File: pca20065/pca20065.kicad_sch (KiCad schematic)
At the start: 7 parts

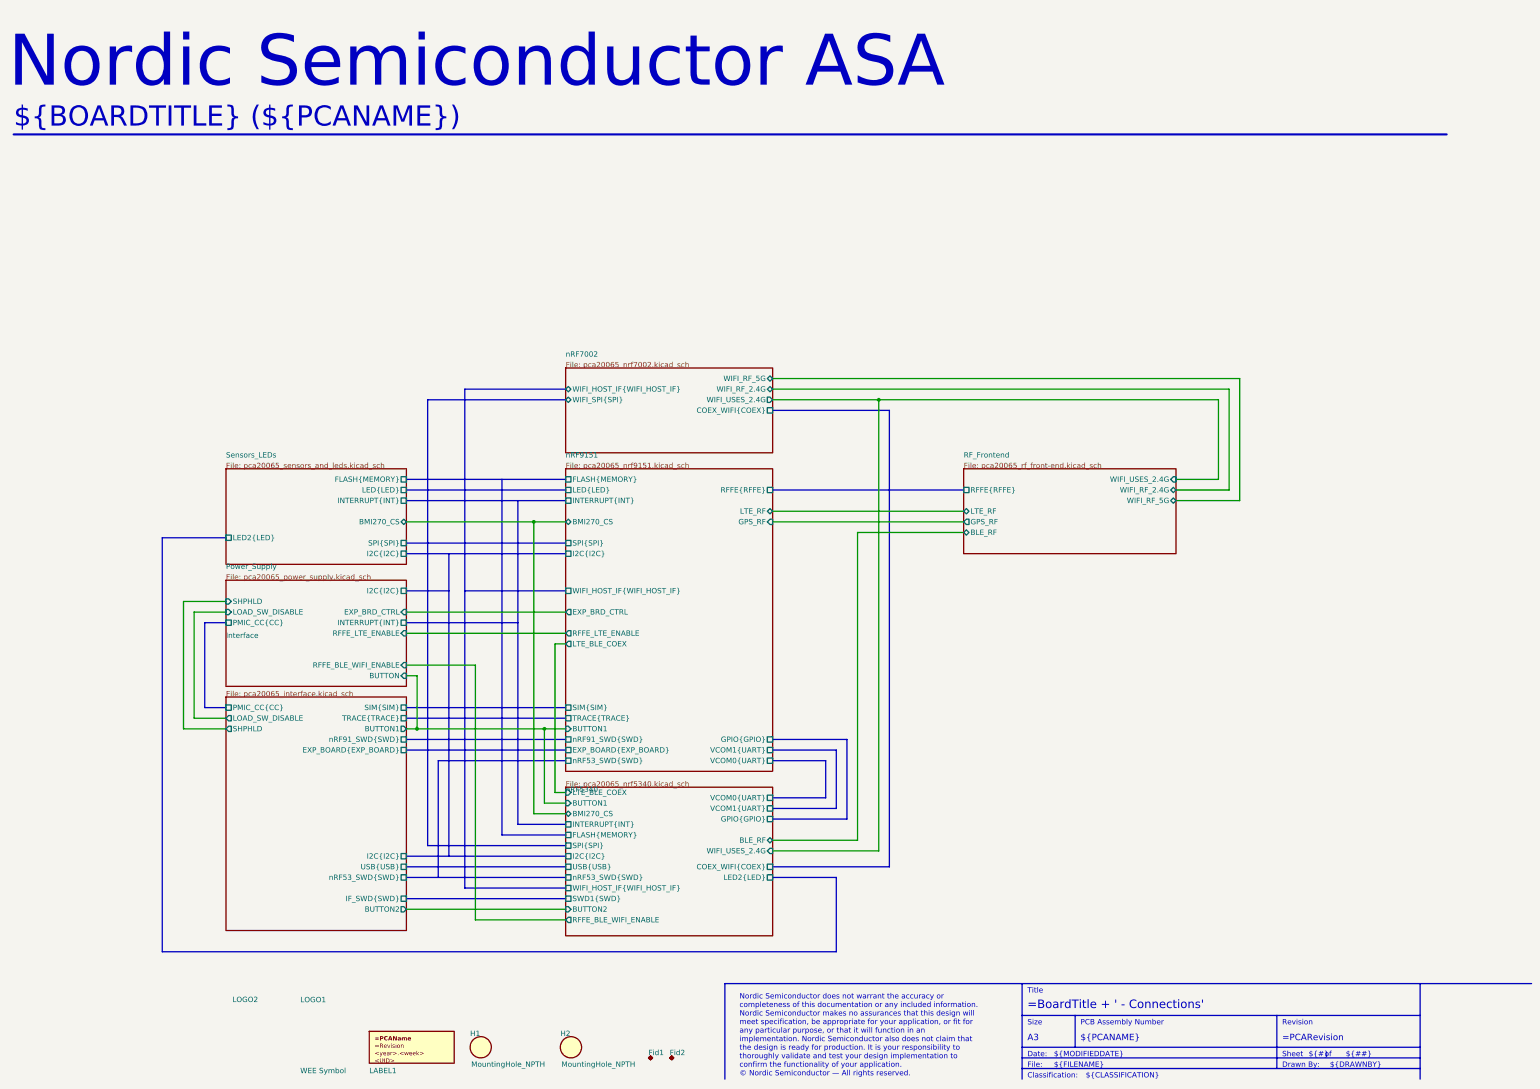
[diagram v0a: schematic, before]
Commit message: Replaced nrf5340 with nrf54l15
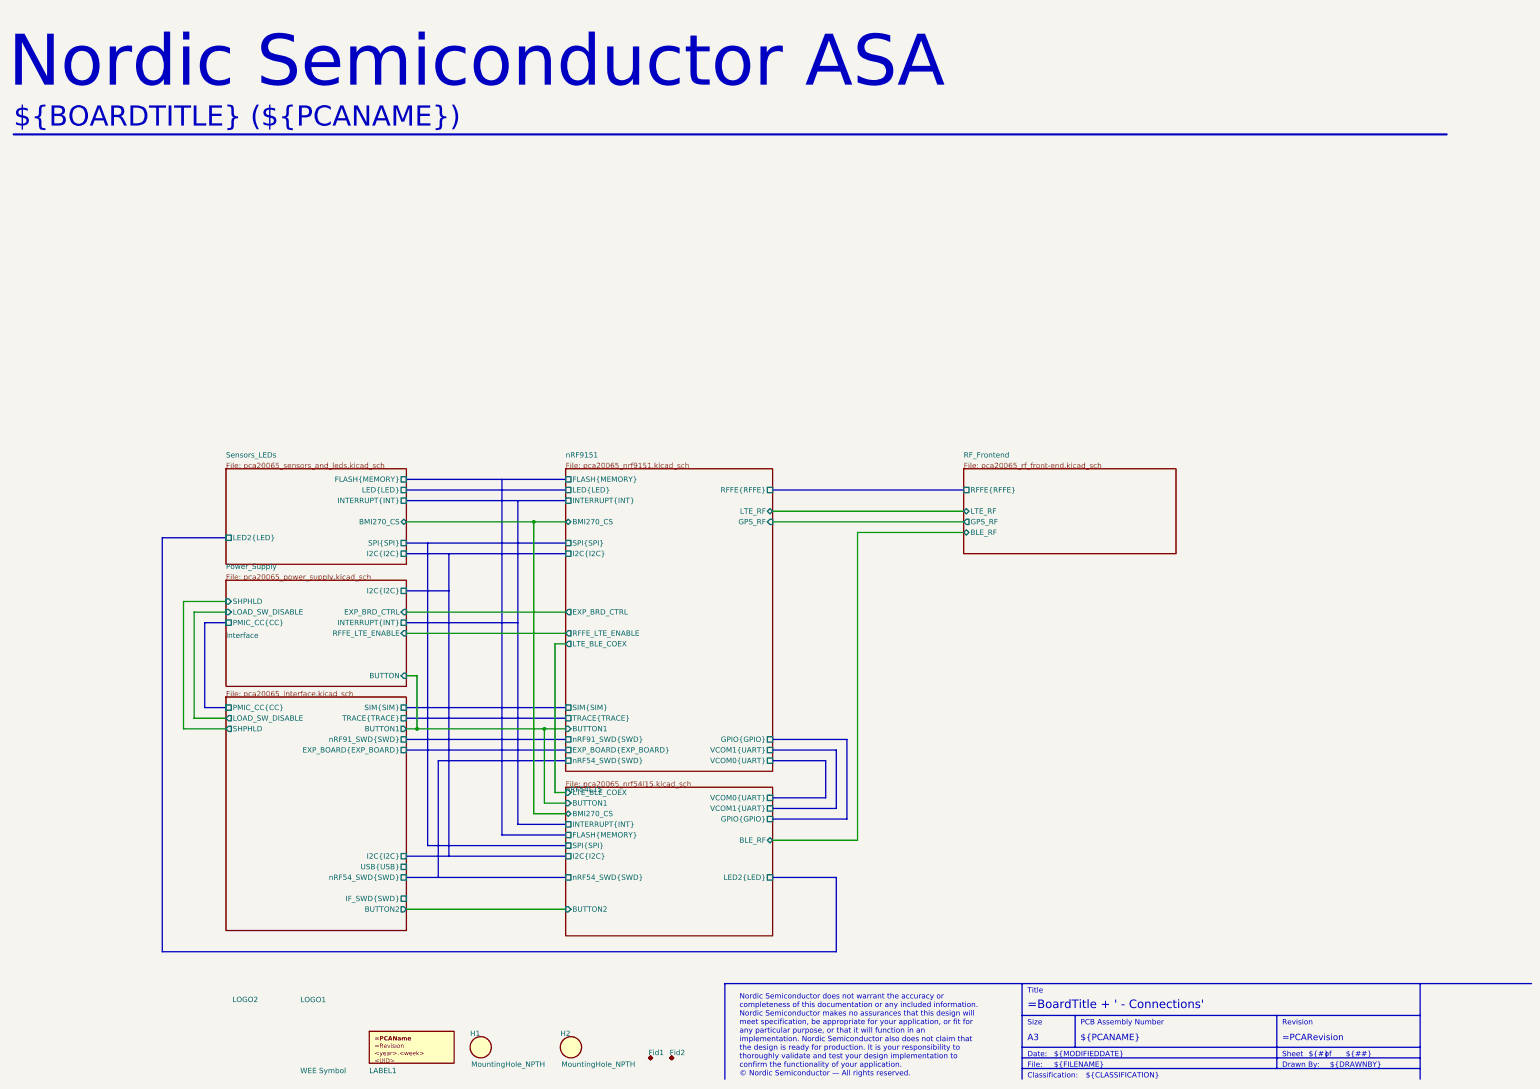
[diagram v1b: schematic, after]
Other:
- sheet nRF5340 renamed nRF54L15
- removed sheet nRF7002
- sheet Interface ports: added nRF54_SWD{SWD}; removed nRF53_SWD{SWD}
- sheet Power_Supply ports: added none; removed RFFE_BLE_WIFI_ENABLE
- sheet RF_Frontend ports: added none; removed WIFI_RF_2.4G, WIFI_RF_5G, WIFI_USES_2.4G
- sheet nRF54L15: file pca20065_nrf5340.kicad_sch -> pca20065_nrf54l15.kicad_sch
- sheet nRF54L15 ports: added nRF54_SWD{SWD}; removed COEX_WIFI{COEX}, RFFE_BLE_WIFI_ENABLE, SWD1{SWD}, USB{USB}, WIFI_HOST_IF{WIFI_HOST_IF}, WIFI_USES_2.4G, nRF53_SWD{SWD}
- sheet nRF9151 ports: added nRF54_SWD{SWD}; removed WIFI_HOST_IF{WIFI_HOST_IF}, nRF53_SWD{SWD}

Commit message: Cleaned up
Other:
- sheet Interface ports: added none; removed IF_SWD{SWD}, TRACE{TRACE}, nRF54_SWD{SWD}, nRF91_SWD{SWD}
- sheet nRF54L15 ports: added nRF91_SWD{SWD}; removed none
- sheet nRF9151 ports: added none; removed TRACE{TRACE}
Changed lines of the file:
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@@
 	(bus
 		(pts
-			(xy 119.38 210.6422) (xy 157.48 210.6422)
-		)
-		(stroke
-			(width 0.508)
-			(type solid)
-			(color 135 186 221 1)
-		)
-	)
-	(bus
-		(pts
 			(xy 71.12 203.0222) (xy 71.12 182.7022)
 		)
@@
 	(bus
 		(pts
-			(xy 119.38 243.6622) (xy 127 243.6622)
-		)
-		(stroke
-			(width 0.508)
-			(type solid)
-			(color 135 186 221 1)
-		)
-	)
-	(bus
-		(pts
 			(xy 207.01 210.6422) (xy 224.79 210.6422)
 		)
@@
 		)
 	)
-	(bus
-		(pts
-			(xy 157.48 205.5622) (xy 119.38 205.5622)
-		)
-		(stroke
-			(width 0.508)
-			(type solid)
-			(color 135 186 221 1)
-		)
-	)
 	(wire
 		(pts
@@
 			)
 		)
+		(pin "nRF91_SWD{SWD}" bidirectional
+			(at 157.48 246.2022 180)
+			(effects
+				(font
+					(size 1.27 1.27)
+				)
+				(justify left)
+			)
+		)
 		(instances
 			(project "pca20065"
@@
 			)
 		)
-		(pin "nRF54_SWD{SWD}" passive
-			(at 119.38 243.6622 0)
-			(effects
-				(font
-					(size 1.27 1.27)
-				)
-				(justify right)
-			)
-		)
-		(pin "nRF91_SWD{SWD}" passive
-			(at 119.38 210.6422 0)
-			(effects
-				(font
-					(size 1.27 1.27)
-				)
-				(justify right)
-			)
-		)
 		(pin "BUTTON1" output
 			(at 119.38 208.1022 0)
@@
 			)
 		)
-		(pin "TRACE{TRACE}" passive
-			(at 119.38 205.5622 0)
-			(effects
-				(font
-					(size 1.27 1.27)
-				)
-				(justify right)
-			)
-		)
-		(pin "IF_SWD{SWD}" passive
-			(at 119.38 248.7422 0)
-			(effects
-				(font
-					(size 1.27 1.27)
-				)
-				(justify right)
-			)
-		)
 		(instances
 			(project "pca20065"
@@
 			)
 		)
-		(pin "TRACE{TRACE}" passive
-			(at 157.48 205.5622 180)
-			(effects
-				(font
-					(size 1.27 1.27)
-				)
-				(justify left)
-			)
-		)
 		(pin "RFFE_LTE_ENABLE" output
 			(at 157.48 185.2422 180)
@@
 		)
 	)
+	(bus
+		(pts
+			(xy 157.48 246.2022) (xy 134.62 246.2022)
+		)
+		(stroke
+			(width 0)
+			(type default)
+		)
+	)
+	(bus
+		(pts
+			(xy 134.62 246.2022) (xy 134.62 210.6422)
+		)
+		(stroke
+			(width 0)
+			(type default)
+		)
+	)
+	(bus
+		(pts
+			(xy 134.62 210.6422) (xy 157.48 210.6422)
+		)
+		(stroke
+			(width 0)
+			(type default)
+		)
+	)
